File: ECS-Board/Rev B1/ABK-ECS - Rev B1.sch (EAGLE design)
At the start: 302 parts, among them J1 USB-B-S-RA, J10 FTSH-105-01-L-DV-NOPASTE, J11 22-05-7028-02, J12 RB1-125BAG1A, J13 22-05-7068-06, J14 22-05-7048-04, J15 22-05-7048-04, J16 22-05-7048-04, J2 MSTBA2, J3 22-05-7068-06, J4 22-05-7028-02, J5 22-05-7068-06, J6 22-05-7068-06, J7 22-05-7068-06, J8 22-05-7028-02, J9 FTSH-103-01-L-DV-NOPASTE, K1 G6K-2G-Y, SW1 B3FS-1015, SW2 B3FS-1015, T1 MMBT2907ALT3, T10 MMBT2222AL, T11 IRLML5103TRPBF, T12 MMBT2222AL, T13 IRLML5103TRPBF, T14 IRLML5103TRPBF, T15 IRLML5103TRPBF, T16 IRLML5103TRPBF, T17 MMBT2222AL, T18 MMBT2222AL, T19 MMBT2222AL, T2 EXMACHINA-LOGO-NAME, T20 MMBT2222AL, T3 IRLML5103TRPBF, T4 IRLML5103TRPBF, T5 IRLML5103TRPBF, T6 IRLML5103TRPBF, T7 MMBT2222AL, T8 MMBT2222AL, T9 MMBT2222AL, U1 AT24C512C-SSHM-B, U10 SN74LVC2G17DBVR, U2 LPC1768FBD100, U3 LT3686HDDPBF, U4 LT3686HDDPBF, U5 CD4050BD, U6 CD4050BD, U7 DP83848JSQ/NOPB, U9 SN74LVC2G17DBVR, X1 FC-135, X2 ASE-12, X3 3000, X4 ASE_50

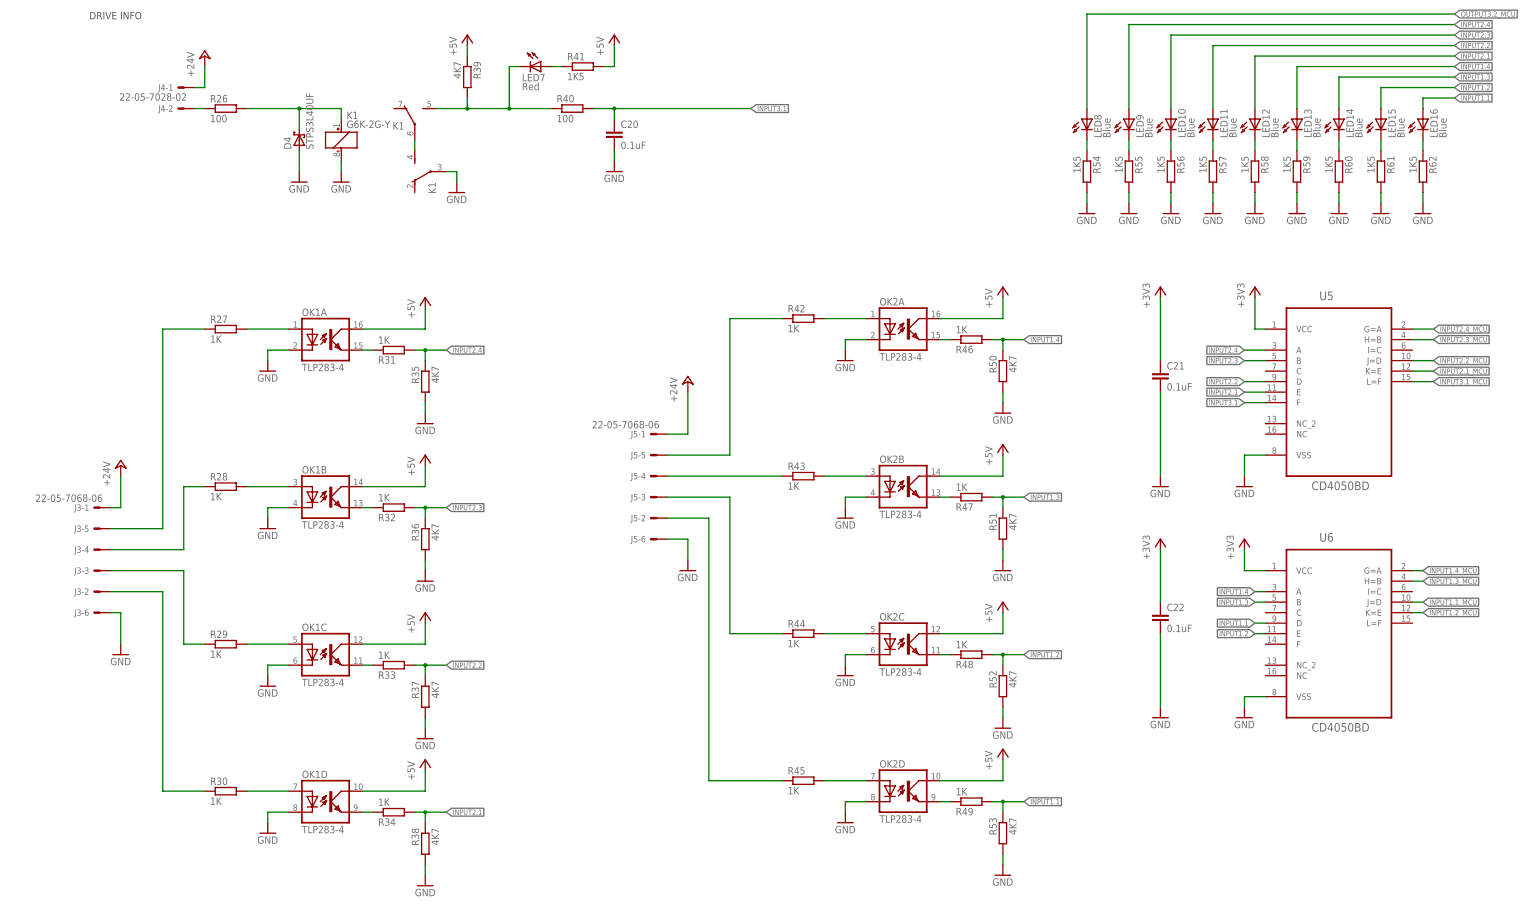
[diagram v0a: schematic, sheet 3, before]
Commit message: Delete realy input
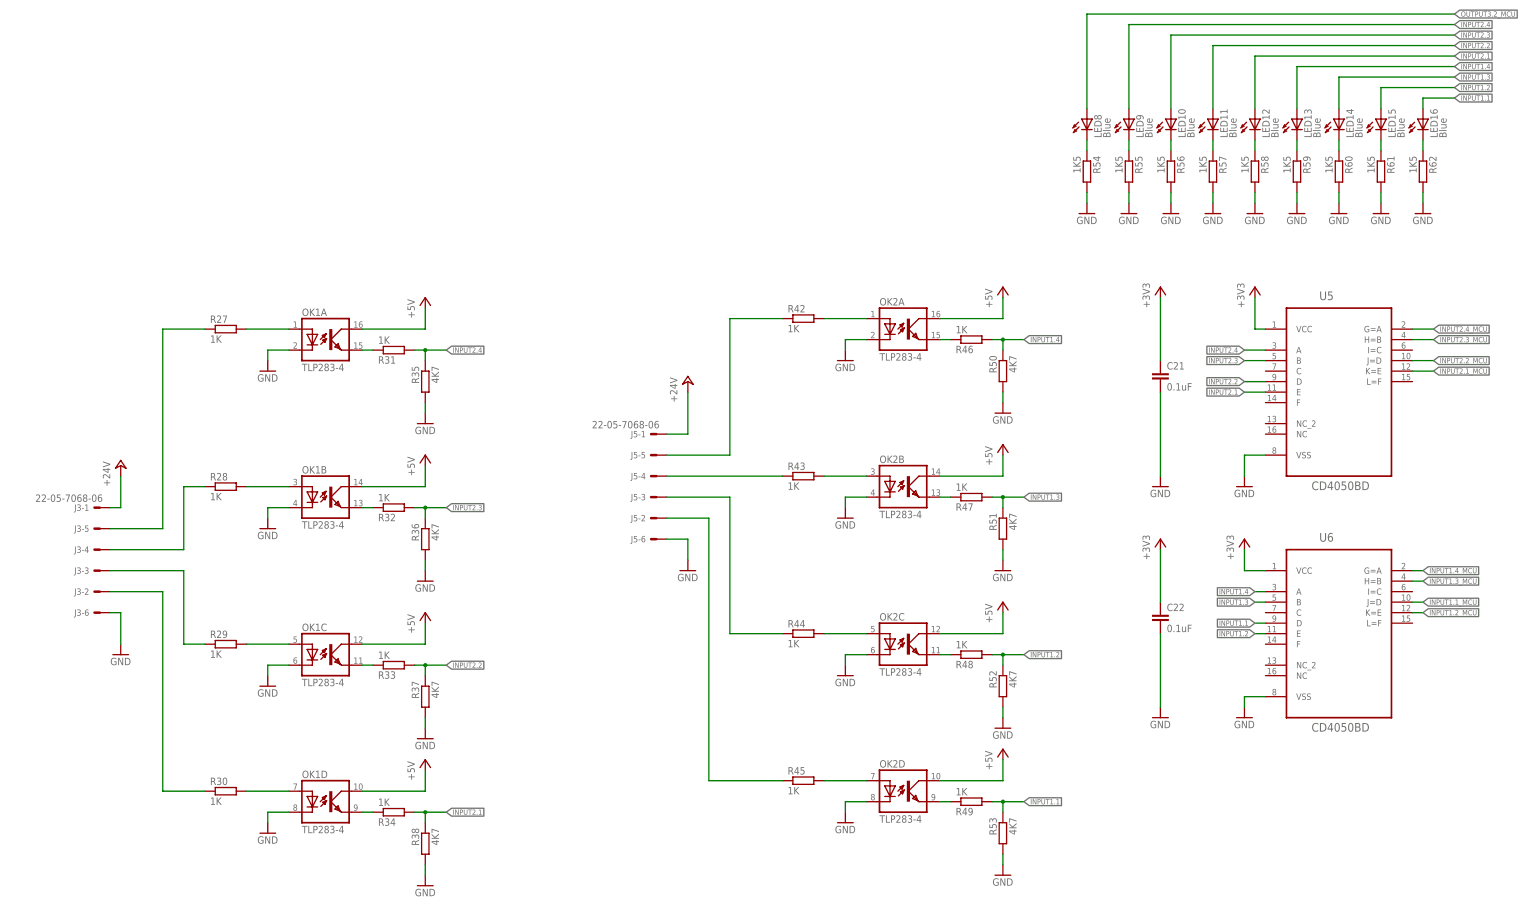
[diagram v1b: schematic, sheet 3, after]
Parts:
- removed C20: 0.1uF, rcl:C-EUC0603
- removed D4: STPS3L40UF, diode:STPS3L40UF
- removed J4: 22-05-7028-02, con-molex:22-05-7028-02
- removed K1: G6K-2G-Y, relay:G6K-2G-Y
- removed LED7: Red, led:LEDCHIPLED_0603
- removed R26, R40: 100, rcl:R-EU_R0603
- removed R39: 4K7, rcl:R-EU_R0603
- removed R41: 1K5, rcl:R-EU_R0603
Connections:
- removed net INPUT3.1: C20.1, R40.2, U5.F
- removed net INPUT3.1_MCU: U2.P0[20]/DTR1/SCL1, U5.L=F
- removed net N$28: D4.C, K11.+, R26.2
- removed net N$32: J4-2.S, R26.1
- removed net N$60: K12.S, K13.P
- removed net N$73: K13.S, LED7.C, R39.2, R40.1
- removed net N$74: LED7.A, R41.1
- net +24V: no longer J4-1.S
- net +5V: no longer R39.1, R41.2
- net GND: no longer C20.2, D4.A, K11.-, K12.P
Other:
- note removed: "DRIVE INFO"

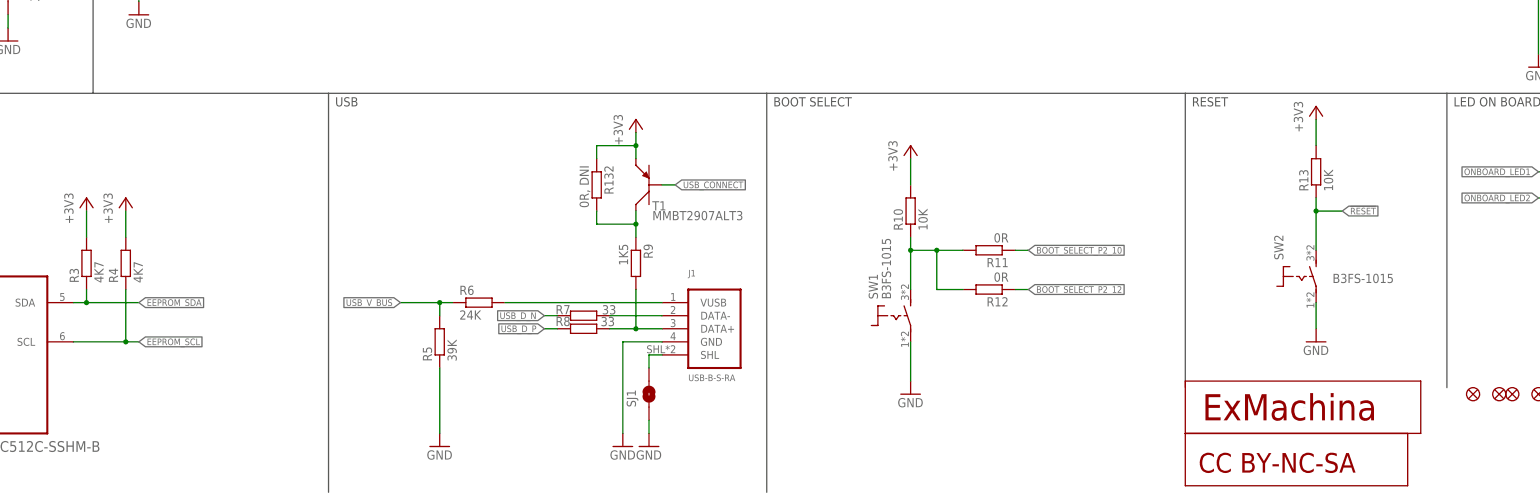
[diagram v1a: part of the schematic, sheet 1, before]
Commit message: Route USB LED, re-place IO leds
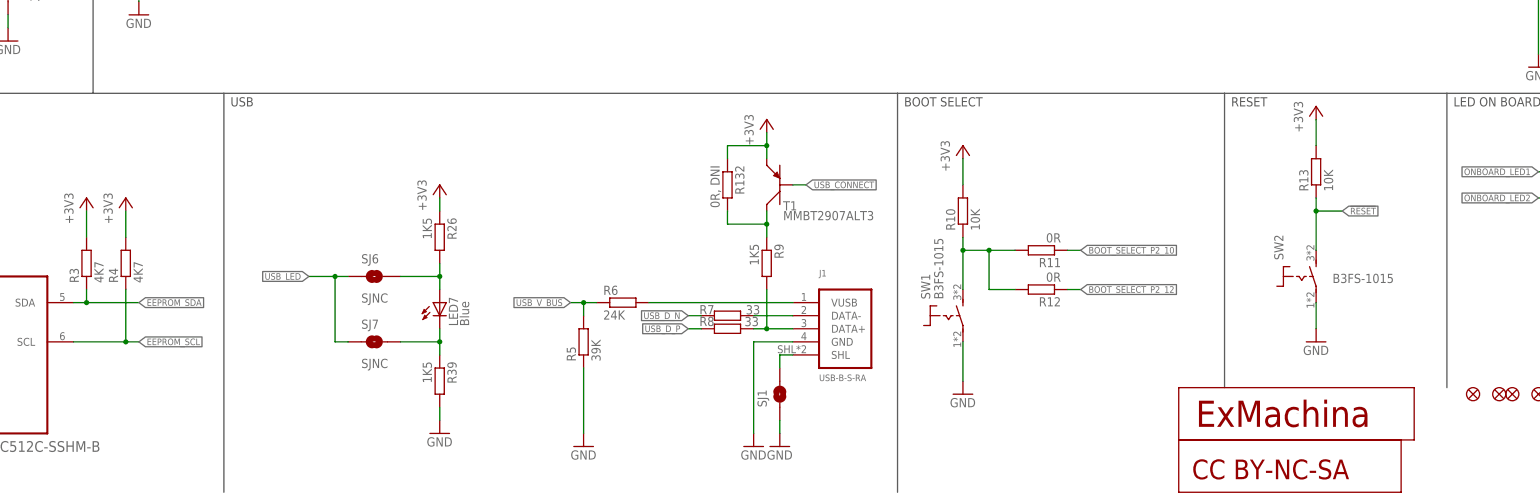
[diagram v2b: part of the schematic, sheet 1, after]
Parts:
- added LED7: Blue, led:LEDCHIPLED_0603
- added R26, R39: 1K5, rcl:R-EU_R0603
- added SJ6, SJ7: SJNC, SparkFun-Passives:SJNC
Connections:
- new net N$28: LED7.A, R26.2, SJ6.2
- new net N$32: LED7.C, R39.1, SJ7.2
- net +3V3: now also R26.1
- net GND: now also R39.2
- net USB_LED: now also SJ6.1, SJ7.1
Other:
- moved on the sheet: J1, R10, R11, R12, R132, R5, R6, R7, R8, R9, SJ1, SW1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

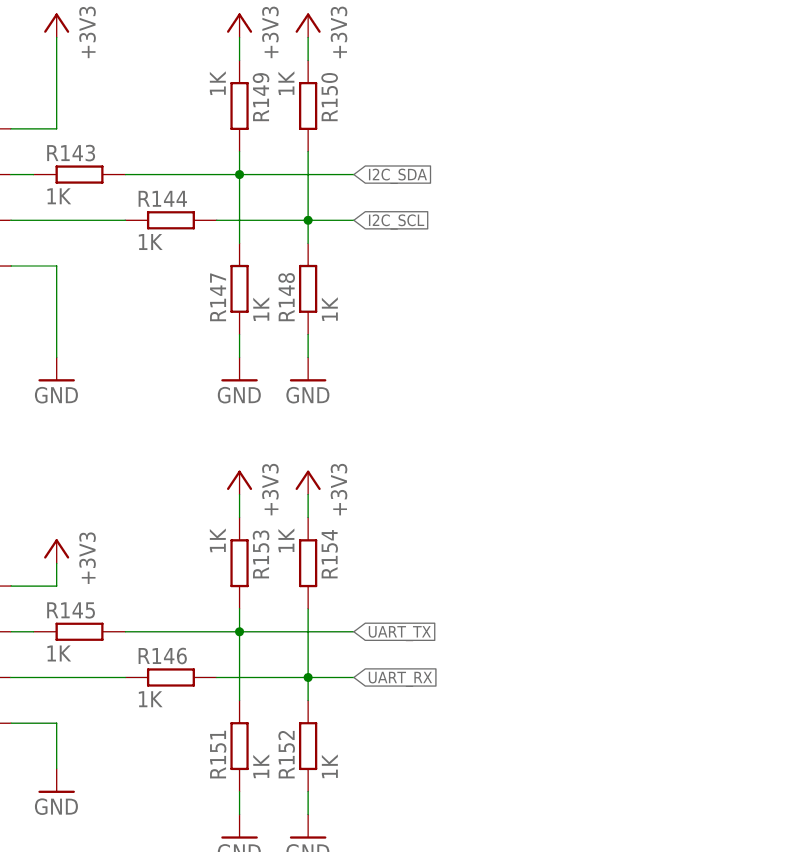
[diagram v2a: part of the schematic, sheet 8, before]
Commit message: Route UART and I2C
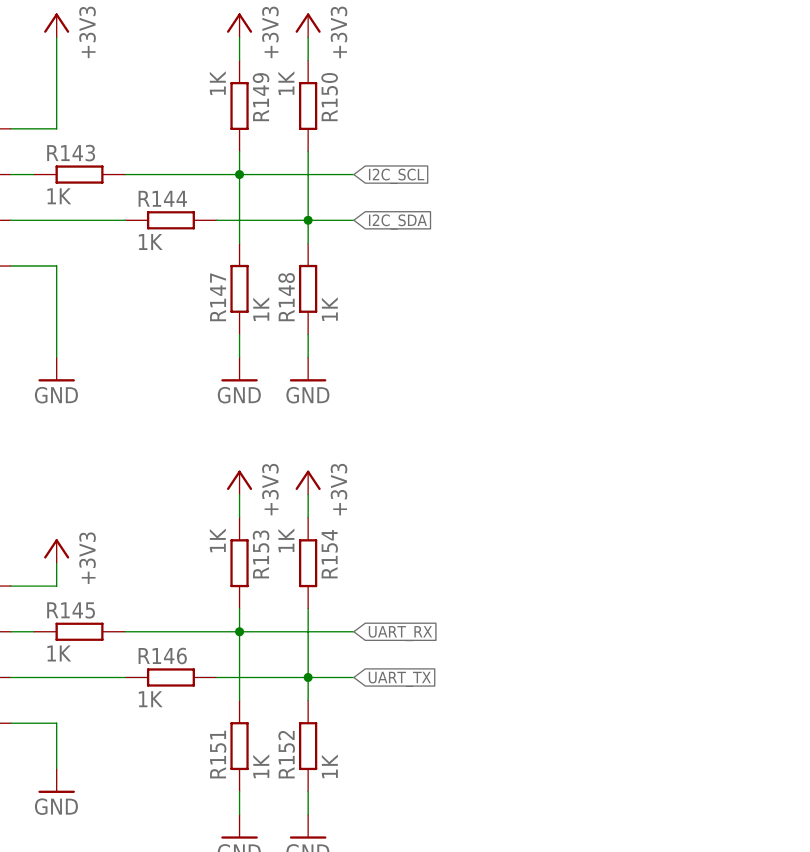
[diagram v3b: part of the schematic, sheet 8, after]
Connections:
- net I2C_SCL: now also R143.2, R147.2, R149.2; no longer R144.2, R148.2, R150.2
- net I2C_SDA: now also R144.2, R148.2, R150.2; no longer R143.2, R147.2, R149.2
- net UART_RX: now also R145.2, R151.2, R153.2; no longer R146.2, R152.2, R154.2
- net UART_TX: now also R146.2, R152.2, R154.2; no longer R145.2, R151.2, R153.2
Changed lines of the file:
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@@
 </segment>
 </net>
-<net name="UART_TX" class="0">
+<net name="UART_RX" class="0">
 <segment>
 <pinref part="R145" gate="G$1" pin="2"/>
@@
 </segment>
 </net>
-<net name="UART_RX" class="0">
-<segment>
-<pinref part="R146" gate="G$1" pin="2"/>
-<wire x1="55.88" y1="40.64" x2="66.04" y2="40.64" width="0.1524" layer="91"/>
-<label x="71.12" y="40.64" size="1.27" layer="95" font="vector" xref="yes"/>
-<pinref part="R152" gate="G$1" pin="2"/>
-<wire x1="66.04" y1="40.64" x2="71.12" y2="40.64" width="0.1524" layer="91"/>
-<wire x1="66.04" y1="38.1" x2="66.04" y2="40.64" width="0.1524" layer="91"/>
-<junction x="66.04" y="40.64"/>
-<pinref part="R154" gate="G$1" pin="2"/>
-<wire x1="66.04" y1="40.64" x2="66.04" y2="48.26" width="0.1524" layer="91"/>
-</segment>
-</net>
 <net name="I2C_SCL" class="0">
-<segment>
-<pinref part="R144" gate="G$1" pin="2"/>
-<wire x1="55.88" y1="91.44" x2="66.04" y2="91.44" width="0.1524" layer="91"/>
-<label x="71.12" y="91.44" size="1.27" layer="95" font="vector" xref="yes"/>
-<pinref part="R148" gate="G$1" pin="2"/>
-<wire x1="66.04" y1="91.44" x2="71.12" y2="91.44" width="0.1524" layer="91"/>
-<wire x1="66.04" y1="88.9" x2="66.04" y2="91.44" width="0.1524" layer="91"/>
-<junction x="66.04" y="91.44"/>
-<pinref part="R150" gate="G$1" pin="2"/>
-<wire x1="66.04" y1="99.06" x2="66.04" y2="91.44" width="0.1524" layer="91"/>
-</segment>
-</net>
-<net name="I2C_SDA" class="0">
 <segment>
 <pinref part="R143" gate="G$1" pin="2"/>
@@
 </segment>
 </net>
+<net name="I2C_SDA" class="0">
+<segment>
+<pinref part="R144" gate="G$1" pin="2"/>
+<wire x1="55.88" y1="91.44" x2="66.04" y2="91.44" width="0.1524" layer="91"/>
+<label x="71.12" y="91.44" size="1.27" layer="95" font="vector" xref="yes"/>
+<pinref part="R148" gate="G$1" pin="2"/>
+<wire x1="66.04" y1="91.44" x2="71.12" y2="91.44" width="0.1524" layer="91"/>
+<wire x1="66.04" y1="88.9" x2="66.04" y2="91.44" width="0.1524" layer="91"/>
+<junction x="66.04" y="91.44"/>
+<pinref part="R150" gate="G$1" pin="2"/>
+<wire x1="66.04" y1="99.06" x2="66.04" y2="91.44" width="0.1524" layer="91"/>
+</segment>
+</net>
+<net name="UART_TX" class="0">
+<segment>
+<pinref part="R146" gate="G$1" pin="2"/>
+<wire x1="55.88" y1="40.64" x2="66.04" y2="40.64" width="0.1524" layer="91"/>
+<label x="71.12" y="40.64" size="1.27" layer="95" font="vector" xref="yes"/>
+<pinref part="R152" gate="G$1" pin="2"/>
+<wire x1="66.04" y1="40.64" x2="71.12" y2="40.64" width="0.1524" layer="91"/>
+<wire x1="66.04" y1="38.1" x2="66.04" y2="40.64" width="0.1524" layer="91"/>
+<junction x="66.04" y="40.64"/>
+<pinref part="R154" gate="G$1" pin="2"/>
+<wire x1="66.04" y1="40.64" x2="66.04" y2="48.26" width="0.1524" layer="91"/>
+</segment>
+</net>

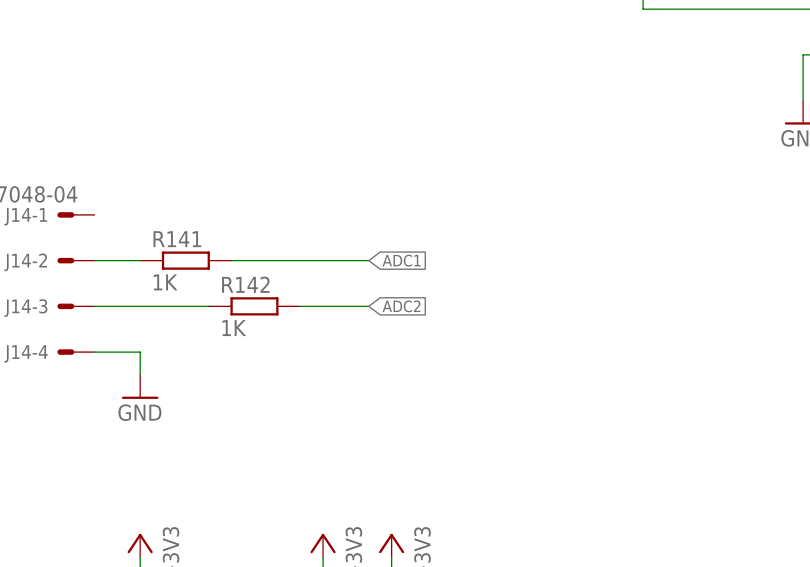
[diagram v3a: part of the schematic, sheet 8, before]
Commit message: Route ADC
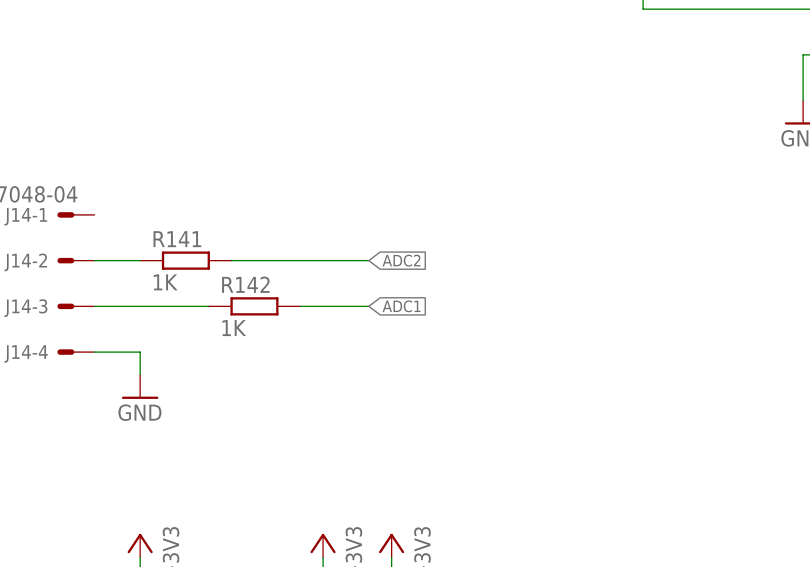
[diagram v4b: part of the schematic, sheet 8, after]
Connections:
- net ADC1: now also R142.2; no longer R141.2
- net ADC2: now also R141.2; no longer R142.2
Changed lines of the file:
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@@
 <net name="ADC2" class="0">
-<segment>
-<pinref part="R142" gate="G$1" pin="2"/>
-<wire x1="55.88" y1="139.7" x2="63.5" y2="139.7" width="0.1524" layer="91"/>
-<label x="63.5" y="139.7" size="1.27" layer="95" font="vector" xref="yes"/>
-</segment>
-</net>
-<net name="ADC1" class="0">
 <segment>
 <pinref part="R141" gate="G$1" pin="2"/>
@@
 </segment>
 </net>
+<net name="ADC1" class="0">
+<segment>
+<pinref part="R142" gate="G$1" pin="2"/>
+<wire x1="55.88" y1="139.7" x2="63.5" y2="139.7" width="0.1524" layer="91"/>
+<label x="63.5" y="139.7" size="1.27" layer="95" font="vector" xref="yes"/>
+</segment>
+</net>
